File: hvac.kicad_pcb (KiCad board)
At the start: 2 copper layers, 191.8 x 114.3 mm, 44 parts, among them IC1 ATMEGA328P-A, J1 PROGRAMMING HEADER, J2 SERIAL PORT, J3 POWER_INPUT, SW1 SPST, SW2 SPST, SW3 SPST, U1 MIC5225, U2 MOSFET_N, U3 MOSFET_N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

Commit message: Add holes to the pcb layout
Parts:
- added H1: hole, homebrew:hole-m2.5, F.Cu at (55.4, 41.5)
- added H2: hole, homebrew:hole-m2.5, F.Cu at (99.1, 60.4)
- added H3: hole, homebrew:hole-m2.5, F.Cu at (53.3, 132.6)
- added H4: hole, homebrew:hole-m2.5, F.Cu at (101.0, 132.4)
- moved J2 165.3 mm to (55.3, 98.4), turned to 90 degrees
- moved R8 118.8 mm to (93.8, 47.9)
- moved D4 118.8 mm to (90.2, 47.9)
- moved J3 116.9 mm to (109.3, 123.7)
- moved JP1 116.9 mm to (109.3, 63.8)
- moved U3 116.9 mm to (96.1, 68.5)
- moved U4 116.9 mm to (96.1, 81.7)
- moved C2 116.9 mm to (61.3, 104.5)
- moved C3 116.9 mm to (74.8, 105.5)
- moved C4 116.9 mm to (95.3, 101.5)
- moved C5 116.9 mm to (94.5, 112.5)
- moved D1 116.9 mm to (88.0, 100.5)
- moved D2 116.9 mm to (88.0, 98.5)
- moved D3 116.9 mm to (88.0, 96.5)
- moved F1 116.9 mm to (112.2, 101.1)
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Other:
- board size 191.8 x 114.3 mm -> 76.5 x 99 mm

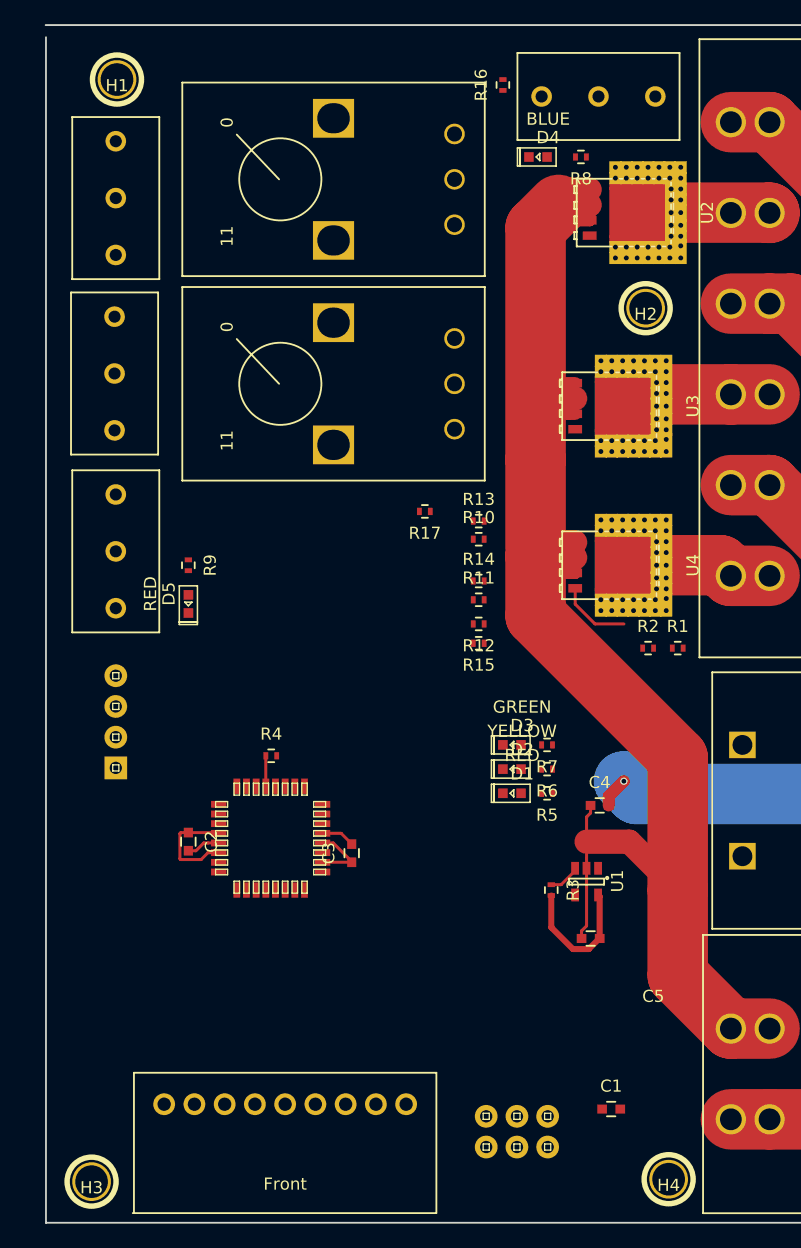
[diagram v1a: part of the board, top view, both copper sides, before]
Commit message: Add fiducials to the board for the pick n place
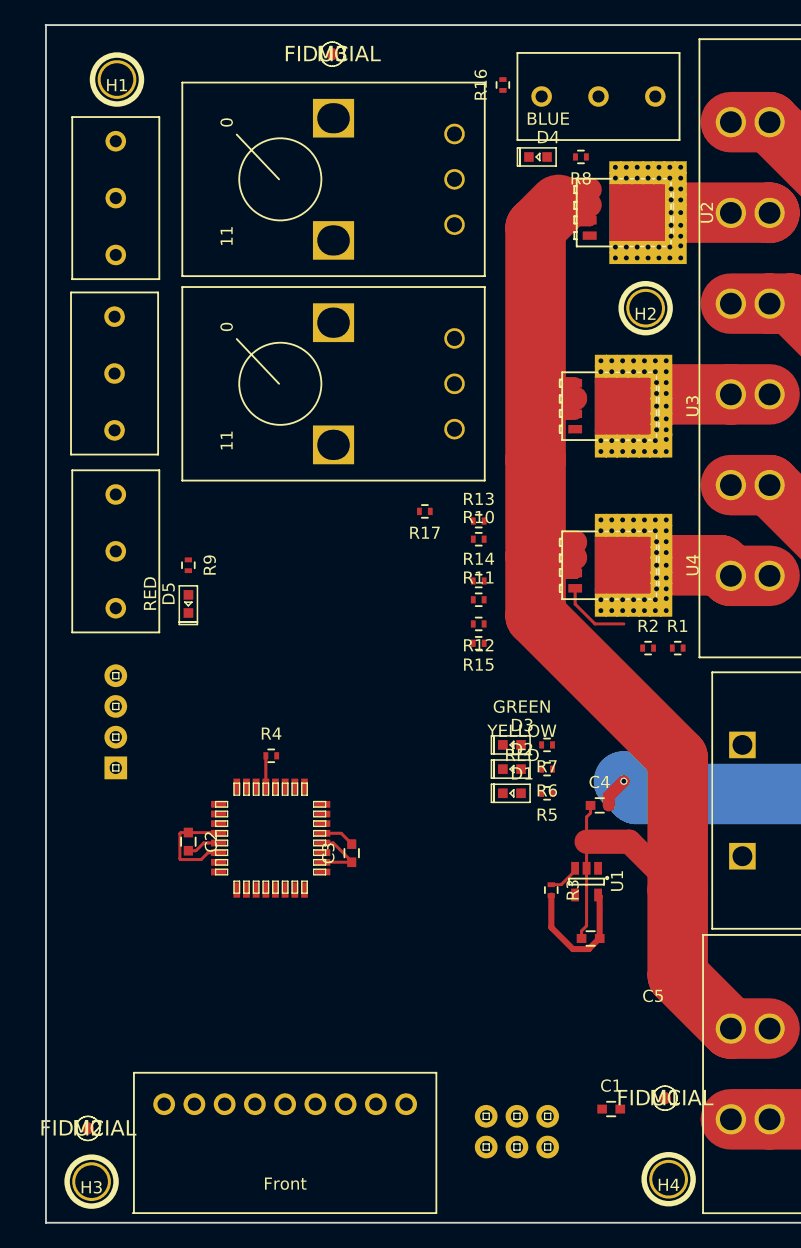
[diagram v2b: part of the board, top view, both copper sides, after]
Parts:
- added M1: FIDUCIAL, FIDUCIAL_1MM, F.Cu at (100.7, 125.7)
- added M2: FIDUCIAL, FIDUCIAL_1MM, F.Cu at (53.0, 128.2)
- added M3: FIDUCIAL, FIDUCIAL_1MM, F.Cu at (73.2, 39.4)
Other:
- outline, holes or cut-outs redrawn

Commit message: Partial routing
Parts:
- moved C1 42.1 mm to (68.0, 95.3), turned to 180 degrees
- moved R5 6.69 mm to (87.8, 94.6), turned to 0 degrees
- moved D1 6.44 mm to (90.7, 94.6), turned to 180 degrees
- moved R7 3.82 mm to (87.8, 98.6), turned to 0 degrees
- moved R6 3.70 mm to (87.8, 96.6), turned to 0 degrees
- moved D3 3.37 mm to (90.7, 98.6), turned to 180 degrees
- moved D2 3.23 mm to (90.7, 96.6), turned to 180 degrees
- moved R15 1.70 mm to (85.3, 86.4)
- moved R12 1.40 mm to (85.3, 87.9), turned to 0 degrees
- turned R13 to 180 degrees
- turned R14 to 180 degrees
- turned SW2 to 90 degrees
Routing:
- net SW_AUTOVENT: track 0.00 -> 91.4 mm, vias 0 -> 2
- net SW_VENT_OVERRIDE: track 0.00 -> 77.7 mm, vias 0 -> 2
- net BTN_TIMER: track 0.00 -> 66.6 mm, vias 0 -> 2
- net SW_SWAMP: track 0.00 -> 64.2 mm, vias 0 -> 3
- net RST: track 2.52 -> 60.1 mm, vias 0 -> 2
- net GND: track 141.1 -> 195.8 mm
- net MOSI: track 0.00 -> 38.1 mm, vias 0 -> 2
- net MISO: track 0.00 -> 36.4 mm, vias 0 -> 2
- net Net-(R13-Pad1): track 0.00 -> 32.4 mm, vias 0 -> 2
- net LED_G: track 0.00 -> 29.7 mm, vias 0 -> 2
- net LED_WATER_LIMIT: track 0.00 -> 27.1 mm, vias 0 -> 2
- net LED_Y: track 0.00 -> 25.3 mm, vias 0 -> 2
- net TEMP_INSIDE: track 0.00 -> 23.7 mm, vias 0 -> 2
- net TEMP_OUTSIDE: track 0.00 -> 22.7 mm
- net LED_R: track 0.00 -> 21.7 mm, vias 0 -> 2
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
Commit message: More routing
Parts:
- moved R2 2.87 mm to (101.8, 90.0), turned to 180 degrees
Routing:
- net LED_TIMER: track 9.30 -> 27.8 mm, vias 0 -> 2
- net +BATT: track 112.0 -> 129.1 mm, vias 1 -> 3
- net POT_TEMP_DIFF: track 0.00 -> 7.32 mm, vias 0 -> 1
- net Net-(R15-Pad1): track 15.2 -> 10.1 mm
- net BATTERY_VOLTAGE_DIVIDER: track 0.00 -> 1.50 mm
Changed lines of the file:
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@@
   (general
     (links 253)
-    (no_connects 204)
+    (no_connects 165)
     (area 47.753858 36.924999 126.075001 136.075001)
     (thickness 1.6)
     (drawings 4)
-    (tracks 321)
+    (tracks 334)
     (zones 0)
     (modules 51)
@@
   )
   (module Resistors_SMD:R_0402 placed (layer F.Cu)
-    (at 99.3 88.5)
+    (at 101.75 90 180)
     (descr "Resistor SMD 0402, reflow soldering, Vishay (see dcrcw.pdf)")
     (tags "resistor 0402")
     (attr smd)
-    (fp_text reference R2 (at 0 -1.8) (layer F.SilkS)
-      (effects (font (size 1 1) (thickness 0.15)))
-    )
-    (fp_text value 4.7k (at 0 1.8) (layer F.Fab)
+    (fp_text reference R2 (at 0 -1.8 180) (layer F.SilkS)
+      (effects (font (size 1 1) (thickness 0.15)))
+    )
+    (fp_text value 4.7k (at 0 1.8 180) (layer F.Fab)
       (effects (font (size 1 1) (thickness 0.15)))
     )
@@
     (fp_line (start 0.25 -0.525) (end -0.25 -0.525) (layer F.SilkS) (width 0.15))
     (fp_line (start -0.25 0.525) (end 0.25 0.525) (layer F.SilkS) (width 0.15))
-    (pad 1 smd rect (at -0.45 0) (size 0.4 0.6) (layers F.Cu F.Paste F.Mask)
+    (pad 1 smd rect (at -0.45 0 180) (size 0.4 0.6) (layers F.Cu F.Paste F.Mask)
       (net 30 BATTERY_VOLTAGE_DIVIDER))
-    (pad 2 smd rect (at 0.45 0) (size 0.4 0.6) (layers F.Cu F.Paste F.Mask)
+    (pad 2 smd rect (at 0.45 0 180) (size 0.4 0.6) (layers F.Cu F.Paste F.Mask)
       (net 1 GND))
     (model Resistors_SMD.3dshapes/R_0402.wrl
@@
   (segment (start 95.275 112.5) (end 95.3 112.5) (width 0.5) (layer F.Cu) (net 5))
   (segment (start 95.166 112.366) (end 95.3 112.5) (width 0.25) (layer F.Cu) (net 5))
+  (via (at 117.3 87.4) (size 0.6) (drill 0.4) (layers F.Cu B.Cu) (net 6))
+  (segment (start 101.724264 87.4) (end 117.3 87.4) (width 0.5) (layer B.Cu) (net 6))
+  (segment (start 101.3 87.4) (end 101.724264 87.4) (width 0.5) (layer B.Cu) (net 6))
+  (segment (start 101.3 88.5) (end 101.3 87.4) (width 0.5) (layer F.Cu) (net 6))
+  (via (at 101.3 87.4) (size 0.6) (drill 0.4) (layers F.Cu B.Cu) (net 6))
   (segment (start 117.3 96.5) (end 117.3 97.456) (width 5) (layer B.Cu) (net 6))
   (segment (start 117.3 97.456) (end 114.199999 100.556001) (width 5) (layer B.Cu) (net 6))
@@
   (segment (start 66.10214 108.5) (end 66.10214 118.69786) (width 0.5) (layer F.Cu) (net 18))
   (segment (start 84.85 78) (end 84.85 79.5) (width 0.5) (layer F.Cu) (net 18))
+  (via (at 77.050001 48.449999) (size 0.6) (drill 0.4) (layers F.Cu B.Cu) (net 19))
+  (segment (start 94.2 49) (end 93.649999 48.449999) (width 0.5) (layer B.Cu) (net 19))
+  (segment (start 93.649999 48.449999) (end 77.050001 48.449999) (width 0.5) (layer B.Cu) (net 19))
+  (segment (start 94.2 47.9) (end 94.2 49) (width 0.5) (layer F.Cu) (net 19))
+  (via (at 94.2 49) (size 0.6) (drill 0.4) (layers F.Cu B.Cu) (net 19))
   (segment (start 66.9 109.3) (end 66.9 117.8) (width 0.5) (layer F.Cu) (net 19))
   (segment (start 66.90224 108.5) (end 66.90224 109.29776) (width 0.5) (layer F.Cu) (net 19))
@@
   (segment (start 85.92 129.74) (end 84.590923 129.74) (width 0.5) (layer F.Cu) (net 24))
   (segment (start 84.590923 129.74) (end 84.4 129.549077) (width 0.5) (layer F.Cu) (net 24))
+  (segment (start 83.3 49.75) (end 76.05 49.75) (width 0.5) (layer B.Cu) (net 27))
+  (segment (start 76.05 49.75) (end 76 49.7) (width 0.5) (layer B.Cu) (net 27))
+  (via (at 76 49.7) (size 0.6) (drill 0.4) (layers F.Cu B.Cu) (net 27))
   (segment (start 75 94.6) (end 75 100.73714) (width 0.5) (layer F.Cu) (net 28))
   (segment (start 75 100.73714) (end 73.52872 102.20842) (width 0.5) (layer F.Cu) (net 28))
@@
   (segment (start 86.112208 94.612208) (end 86.1 94.6) (width 0.5) (layer F.Cu) (net 28))
   (via (at 86.1 94.6) (size 0.6) (drill 0.4) (layers F.Cu B.Cu) (net 28))
+  (segment (start 102.2 88.5) (end 102.2 90) (width 0.5) (layer F.Cu) (net 30))
   (segment (start 62.339999 89.139999) (end 62.339999 81.439999) (width 0.5) (layer F.Cu) (net 32))
   (segment (start 62.339999 81.439999) (end 62.1 81.2) (width 0.5) (layer F.Cu) (net 32))
@@
   (segment (start 86.65 82.95) (end 86.7 82.9) (width 0.5) (layer F.Cu) (net 41))
   (via (at 86.7 82.9) (size 0.6) (drill 0.4) (layers F.Cu B.Cu) (net 41))
-  (segment (start 94.914998 86.5) (end 94.921328 86.49367) (width 0.25) (layer F.Cu) (net 42))
-  (segment (start 94.921328 86.49367) (end 97.3 86.5) (width 0.25) (layer F.Cu) (net 42))
-  (segment (start 86.7 86.4) (end 94.827658 86.4) (width 0.5) (layer B.Cu) (net 42))
-  (segment (start 94.827658 86.4) (end 94.921328 86.49367) (width 0.5) (layer B.Cu) (net 42))
-  (via (at 94.921328 86.49367) (size 0.6) (drill 0.4) (layers F.Cu B.Cu) (net 42))
-  (segment (start 85.75 86.4) (end 86.7 86.4) (width 0.5) (layer F.Cu) (net 42))
-  (via (at 86.7 86.4) (size 0.6) (drill 0.4) (layers F.Cu B.Cu) (net 42))
-  (segment (start 93.275 83.555) (end 93.275 84.860002) (width 0.25) (layer F.Cu) (net 42))
-  (segment (start 93.275 84.860002) (end 94.914998 86.5) (width 0.25) (layer F.Cu) (net 42))
+  (segment (start 93.275 83.555) (end 93.310356 84.882698) (width 0.5) (layer F.Cu) (net 42))
+  (segment (start 93.275 84.918054) (end 93.310356 84.882698) (width 0.5) (layer F.Cu) (net 42))
+  (via (at 93.310356 84.882698) (size 0.6) (drill 0.4) (layers F.Cu B.Cu) (net 42))
+  (segment (start 92.6 85.6) (end 93.3 84.9) (width 0.5) (layer B.Cu) (net 42))
+  (segment (start 85.75 85.6) (end 92.6 85.6) (width 0.5) (layer B.Cu) (net 42))
+  (segment (start 85.8 85.55) (end 85.75 85.6) (width 0.5) (layer F.Cu) (net 42))
+  (via (at 85.75 85.6) (size 0.6) (drill 0.4) (layers F.Cu B.Cu) (net 42))
+  (segment (start 85.75 86.4) (end 85.75 85.6) (width 0.5) (layer F.Cu) (net 42))
   (segment (start 87.3 44.9) (end 86.2 46) (width 0.5) (layer F.Cu) (net 43))
   (segment (start 86.2 46) (end 83.3 46) (width 0.5) (layer F.Cu) (net 43))

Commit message: First pass routing everything
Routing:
- net SIGNAL_PUMP: track 11.7 -> 94.3 mm, vias 0 -> 5
- net LED_TIMER: track 27.8 -> 108.0 mm, vias 2 -> 4
- net SIGNAL_VENT_FAN: track 12.6 -> 88.3 mm, vias 0 -> 4
- net SW_WATER_LIMIT: track 0.00 -> 55.7 mm, vias 0 -> 3
- net POT_TEMP_DIFF: track 7.32 -> 62.9 mm
- net POT_VENT_SPEED: track 0.00 -> 51.5 mm, vias 0 -> 2
- net SCK: track 0.00 -> 43.4 mm, vias 0 -> 4
- net BATTERY_VOLTAGE_DIVIDER: track 1.50 -> 43.8 mm, vias 0 -> 2
- net SIGNAL_SWAMP_FAN: track 1.50 -> 37.2 mm, vias 0 -> 2
- net AUX: track 0.00 -> 34.2 mm, vias 0 -> 2
- net VCC: track 41.2 -> 70.6 mm, vias 0 -> 4
- net GND: track 195.8 -> 215.5 mm, vias 0 -> 6
- net BTN_TIMER: track 66.6 -> 84.4 mm, vias 2 -> 4
- added copper zone on B.Cu, net GND
- added copper zone on F.Cu, net VCC
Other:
- net class Default: trace_width 0.25 -> 0.5
- rule trace_min: 0.2 -> 0.25

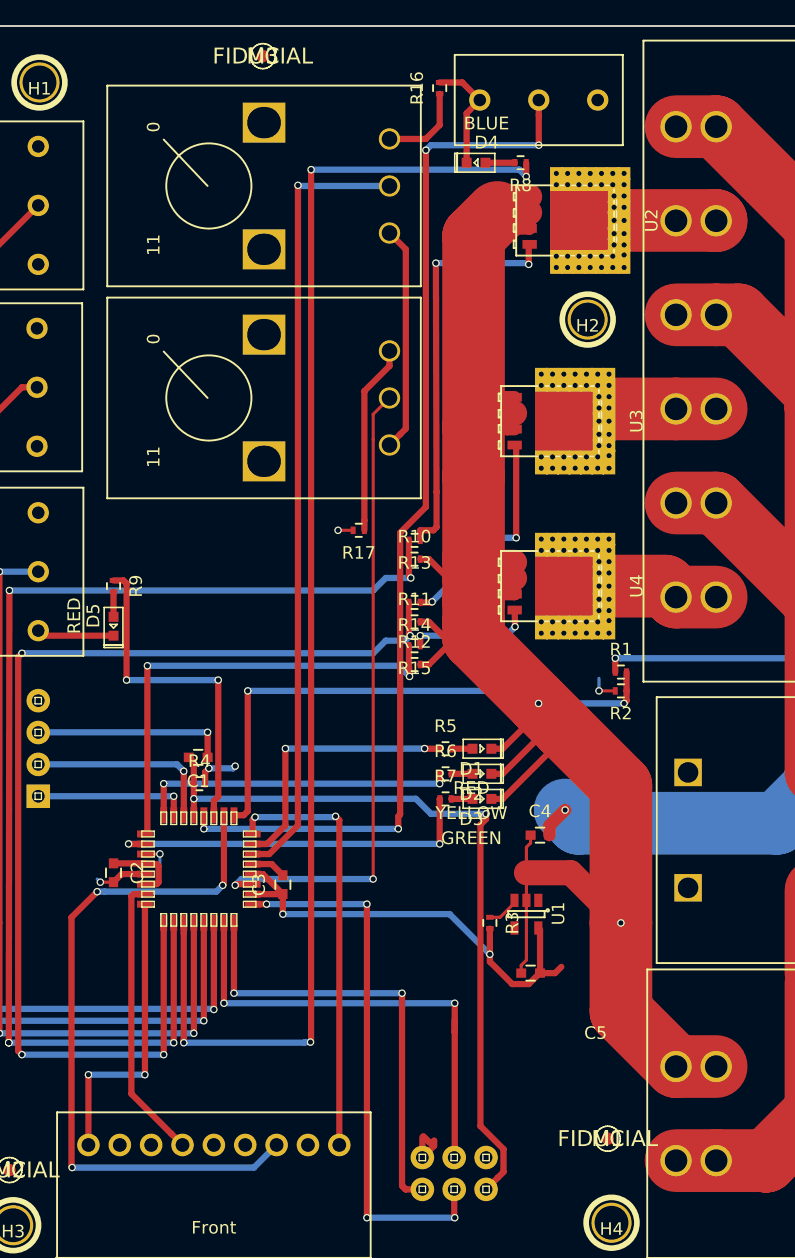
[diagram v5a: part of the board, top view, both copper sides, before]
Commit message: Fix remaining DRC errors
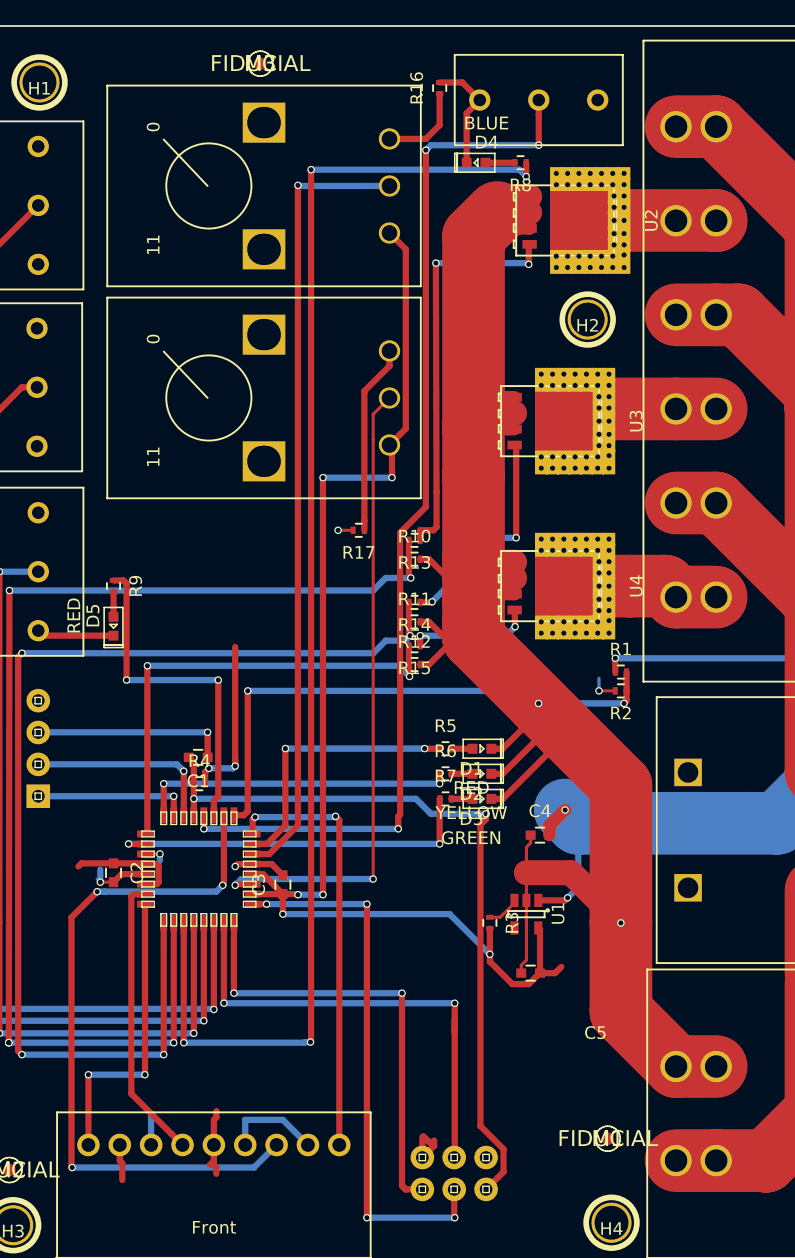
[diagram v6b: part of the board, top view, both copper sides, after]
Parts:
- moved M3 0.63 mm to (73.0, 40.0)
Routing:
- net OUT_VENT_FAN: track 11.0 -> 114.7 mm
- net OUT_PUMP: track 9.40 -> 102.6 mm
- net OUT_SWAMP_FAN: track 11.0 -> 90.3 mm
- net VCC: track 70.6 -> 136.6 mm, vias 4 -> 8
- net GND: track 215.5 -> 228.7 mm, vias 6 -> 7
- net +BATT: track 129.1 -> 137.8 mm, vias 3 -> 4
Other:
- rule trace_min: 0.25 -> 0.13
- rule via_min_drill: 0.3 -> 0.305
- rule via_min_size: 0.4 -> 0.465

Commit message: Add version info to the board
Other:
- board text added: "CAL"
- board text added: "HVAC V1.0"
- board text added: "TEST"
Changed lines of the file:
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@@
     (area 47.753858 36.924999 126.075001 136.075001)
     (thickness 1.6)
-    (drawings 4)
+    (drawings 16)
     (tracks 702)
     (zones 0)
@@
     (visible_elements FFFFFF7F)
     (pcbplotparams
-      (layerselection 0x00030_80000001)
-      (usegerberextensions false)
+      (layerselection 0x010fc_80000001)
+      (usegerberextensions true)
       (excludeedgelayer true)
       (linewidth 0.100000)
@@
       (psnegative false)
       (psa4output false)
-      (plotreference true)
-      (plotvalue true)
+      (plotreference false)
+      (plotvalue false)
       (plotinvisibletext false)
       (padsonsilk false)
@@
       (outputformat 1)
       (mirror false)
-      (drillshape 1)
+      (drillshape 0)
       (scaleselection 1)
       (outputdirectory ""))
@@
     (pad 1 smd circle (at 0 0) (size 0.99822 0.99822) (layers F.Cu F.Paste F.Mask))
   )
+  (gr_text TEST (at 53 119 270) (layer F.SilkS)
+    (effects (font (size 1.5 1.5) (thickness 0.3)))
+  )
+  (gr_text CAL (at 53 111 270) (layer F.SilkS)
+    (effects (font (size 1.5 1.5) (thickness 0.3)))
+  )
+  (gr_line (start 52 116) (end 52 114) (layer F.SilkS) (width 0.2))
+  (gr_line (start 54 116) (end 52 116) (layer F.SilkS) (width 0.2))
+  (gr_line (start 54 114) (end 54 116) (layer F.SilkS) (width 0.2))
+  (gr_line (start 52 114) (end 54 114) (layer F.SilkS) (width 0.2))
+  (gr_line (start 52 106) (end 53 106) (layer F.SilkS) (width 0.2))
+  (gr_line (start 52 108) (end 52 106) (layer F.SilkS) (width 0.2))
+  (gr_line (start 54 108) (end 52 108) (layer F.SilkS) (width 0.2))
+  (gr_line (start 54 106) (end 54 108) (layer F.SilkS) (width 0.2))
+  (gr_line (start 53 106) (end 54 106) (layer F.SilkS) (width 0.2))
+  (gr_text "HVAC V1.0" (at 56 112 270) (layer F.SilkS)
+    (effects (font (size 1.5 1.5) (thickness 0.3)))
+  )
   (gr_line (start 49.53 136) (end 49.53 37) (angle 90) (layer Edge.Cuts) (width 0.15))
   (gr_line (start 126 136) (end 49.53 136) (angle 90) (layer Edge.Cuts) (width 0.15))
@@
       )
     )
+  )
+  (zone (net 5) (net_name VCC) (layer F.SilkS) (hatch edge 0.508)
+    (connect_pads (clearance 0.75))
+    (min_thickness 0.254)
+    (fill yes (arc_segments 16) (thermal_gap 0.508) (thermal_bridge_width 0.508))
+    (polygon
+      (pts
+        (xy 52 106) (xy 54 106) (xy 54 108) (xy 52 108)
+      )
+    )
+  )
+  (zone (net 5) (net_name VCC) (layer F.SilkS) (hatch edge 0.508)
+    (connect_pads (clearance 0.75))
+    (min_thickness 0.254)
+    (fill yes (arc_segments 16) (thermal_gap 0.508) (thermal_bridge_width 0.508))
+    (polygon
+      (pts
+        (xy 52 114) (xy 54 114) (xy 54 116) (xy 52 116)
+      )
+    )

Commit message: Move pieces to fit better
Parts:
- BTN1: footprint homebrew:EG2355-ND -> homebrew:PVA1-OA-H2
- moved F1 4.00 mm to (116.2, 101.1)
- moved R8 1.85 mm to (92.0, 48.5)
- moved BTN1 1.84 mm to (97.0, 42.5), turned to 180 degrees
- moved D4 0.95 mm to (89.3, 48.0)
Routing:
- net +BATT: track 137.8 -> 143.3 mm
- net BTN_TIMER: track 84.4 -> 80.2 mm, vias 4 -> 3
- net Net-(F1-Pad1): track 29.7 -> 32.3 mm
- net GND: track 228.7 -> 227.0 mm
- net SIGNAL_PUMP: track 94.3 -> 93.1 mm
- net LED_TIMER: track 108.0 -> 108.8 mm
- net Net-(D4-PadANOD): track 2.35 -> 1.76 mm
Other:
- board text added: "GND"
- board text added: "RST"
- board text added: "RXI"
- board text added: "TXO"
